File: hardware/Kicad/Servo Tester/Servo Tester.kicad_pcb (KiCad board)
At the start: 2 copper layers, 135 x 75 mm, 58 parts, among them J1 Servo 1, J2 Servo 2, J3 Servo 3, J4 XT60PW-M, SW1 SS-12D11, SW2 STD / HV, SW3 SW_Push - Up, SW4 SW_Push - Select, SW5 SW_Push - Down, U1 Mini360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

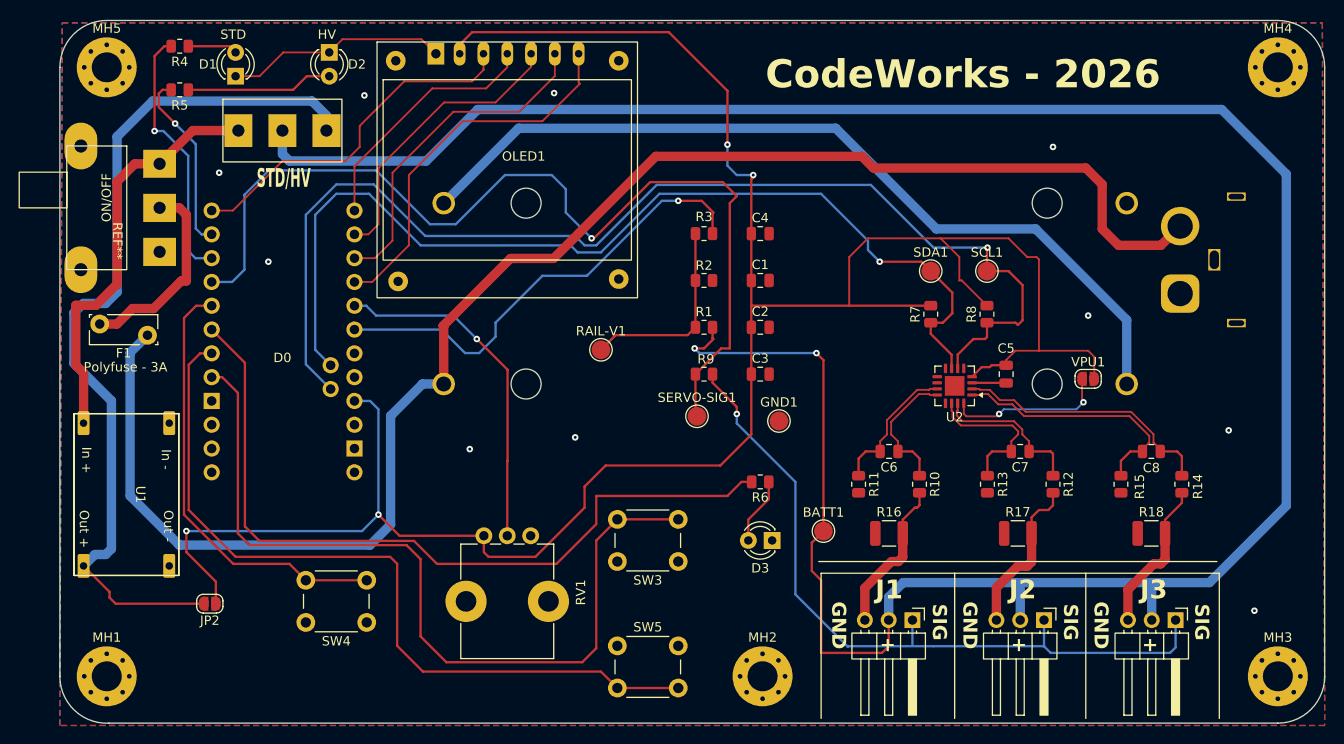
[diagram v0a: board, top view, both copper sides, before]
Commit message: Add designators, netlist, positions, and symbol library for Servo Tester project
- Created designators.csv to define component designators for the Servo Tester.
- Added netlist.ipc to specify the electrical connections and layout of the circuit.
- Introduced positions.csv to provide the coordinates and rotation for each component on the PCB.
- Established sym-lib-table to include the Servo Tester symbol library in KiCad.
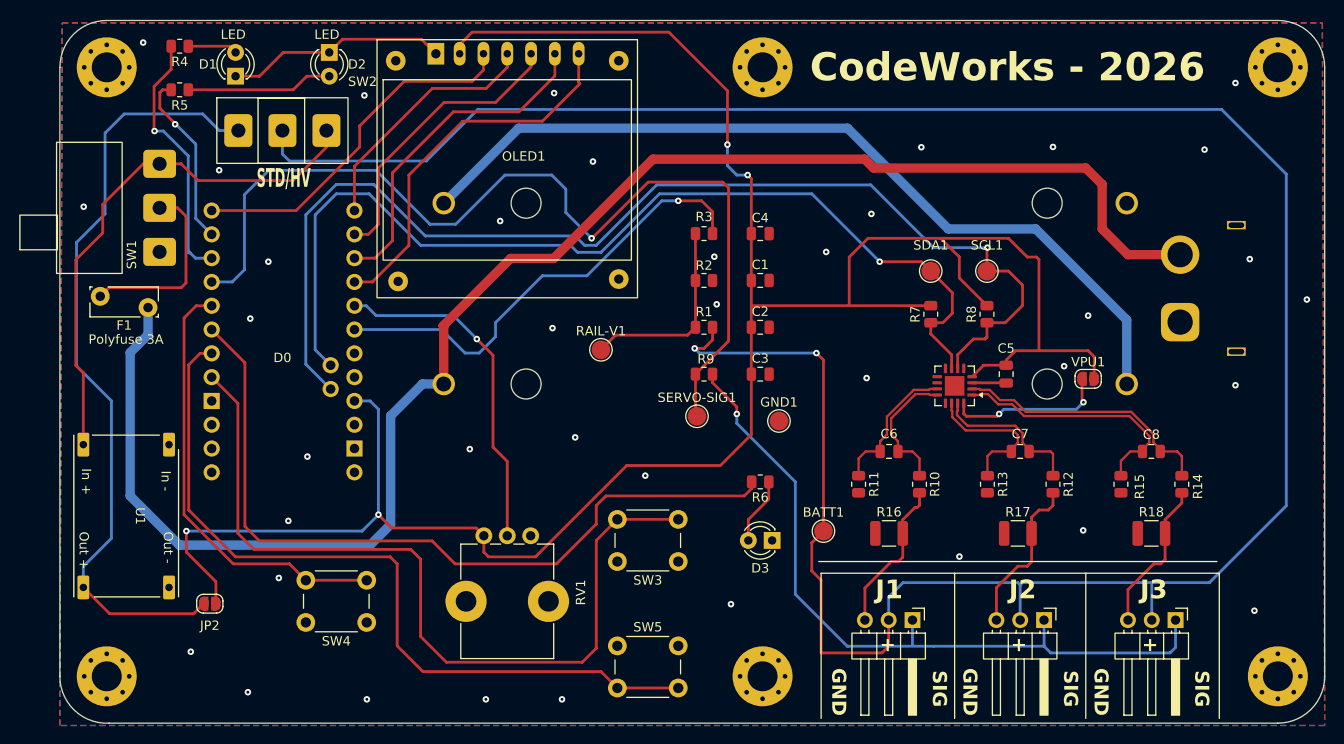
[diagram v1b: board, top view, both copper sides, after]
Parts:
- added MH6: ~, Servo Tester:MountingHole_3.2mm_M3_Pad_Via, F.Cu at (164.8, 60.8)
- A1: footprint CodeWorks-Essentials:Clone_Pro_Mini_Socket_No_PROG -> Servo Tester:Clone_Pro_Mini_Socket_No_PROG
- BATT1: value BATT -> TestPoint; footprint TestPoint:TestPoint_Pad_D2.0mm -> Servo Tester:TestPoint_Pad_D2.0mm
- BT1: footprint CodeWorks-Essentials:BAT_BK-18650-PC4 -> Servo Tester:BAT_BK-18650-PC4
- C1, C2, C5: value 100nF -> C; footprint Capacitor_SMD:C_0805_2012Metric -> Servo Tester:C_0805_2012Metric
- C3, C6, C8: value 0.1uF -> C; footprint Capacitor_SMD:C_0805_2012Metric -> Servo Tester:C_0805_2012Metric
- C4: value 10uF -> C; footprint Capacitor_SMD:C_0805_2012Metric -> Servo Tester:C_0805_2012Metric
- C7: value 0.1uf -> C; footprint Capacitor_SMD:C_0805_2012Metric -> Servo Tester:C_0805_2012Metric
- D1: value STD -> LED; footprint LED_THT:LED_D3.0mm -> Servo Tester:LED_D3.0mm
- D2: value HV -> LED; footprint LED_THT:LED_D3.0mm -> Servo Tester:LED_D3.0mm
- D3: value ALERT -> LED; footprint LED_THT:LED_D3.0mm -> Servo Tester:LED_D3.0mm
- F1: value Polyfuse - 3A -> Polyfuse 3A; footprint Fuse:Fuse_Bourns_MF-RG300 -> Servo Tester:Fuse_LittleFuseRUEF300
- GND1: value GND -> TestPoint; footprint TestPoint:TestPoint_Pad_D2.0mm -> Servo Tester:TestPoint_Pad_D2.0mm
- J1: value Servo 1 -> Conn_01x03_Pin; footprint Connector_PinHeader_2.54mm:PinHeader_1x03_P2.54mm_Horizontal -> Servo Tester:PinHeader_1x03_P2.54mm_Horizontal
- J2: value Servo 2 -> Conn_01x03_Pin; footprint Connector_PinHeader_2.54mm:PinHeader_1x03_P2.54mm_Horizontal -> Servo Tester:PinHeader_1x03_P2.54mm_Horizontal
- J3: value Servo 3 -> Conn_01x03_Pin; footprint Connector_PinHeader_2.54mm:PinHeader_1x03_P2.54mm_Horizontal -> Servo Tester:PinHeader_1x03_P2.54mm_Horizontal
- J4: footprint Connector_AMASS:AMASS_XT60IPW-M_1x03_P7.20mm_Horizontal -> Servo Tester:AMASS_XT60PW-M_1x02_P7.20mm_Horizontal
- JP2: value 5V -> SolderJumper_2_Open; footprint Jumper:SolderJumper-2_P1.3mm_Open_RoundedPad1.0x1.5mm -> Servo Tester:SolderJumper-2_P1.3mm_Open_RoundedPad1.0x1.5mm
- MH1, MH2, MH3, MH4, MH5: value M3 -> ~; footprint MountingHole:MountingHole_3.2mm_M3_Pad_Via -> Servo Tester:MountingHole_3.2mm_M3_Pad_Via
- OLED1: footprint CodeWorks-Essentials:OLED_0.96_SPI_Module_1x07_P2.54mm -> Servo Tester:OLED_0.96_SPI_Module_1x07_P2.54mm
- R1: value 47K -> R; footprint Resistor_SMD:R_0805_2012Metric -> Servo Tester:R_0805_2012Metric
- R10, R11, R12, R13, R14, R15: value 10R -> R; footprint Resistor_SMD:R_0805_2012Metric -> Servo Tester:R_0805_2012Metric
- R16, R17, R18: value 0.1R -> R; footprint Resistor_SMD:R_1210_3225Metric -> Servo Tester:R_1210_3225Metric
- R2: value 27K -> R; footprint Resistor_SMD:R_0805_2012Metric -> Servo Tester:R_0805_2012Metric
- R3: value 0R -> R; footprint Resistor_SMD:R_0805_2012Metric -> Servo Tester:R_0805_2012Metric
- R4, R5: value 1K -> R; footprint Resistor_SMD:R_0805_2012Metric -> Servo Tester:R_0805_2012Metric
- R6: value 470R -> R; footprint Resistor_SMD:R_0805_2012Metric -> Servo Tester:R_0805_2012Metric
- R7, R8: value 4.7K -> R; footprint Resistor_SMD:R_0805_2012Metric -> Servo Tester:R_0805_2012Metric
- R9: value 330R -> R; footprint Resistor_SMD:R_0805_2012Metric -> Servo Tester:R_0805_2012Metric
- RAIL-V1: value ~ -> TestPoint; footprint TestPoint:TestPoint_Pad_D2.0mm -> Servo Tester:TestPoint_Pad_D2.0mm
- RV1: footprint Potentiometer_THT:Potentiometer_Bourns_PTV09A-1_Single_Vertical -> Servo Tester:Potentiometer_Bourns_PTV09A-1_Single_Vertical
- SCL1: value SCL -> TestPoint; footprint TestPoint:TestPoint_Pad_D2.0mm -> Servo Tester:TestPoint_Pad_D2.0mm
- SDA1: value SDA -> TestPoint; footprint TestPoint:TestPoint_Pad_D2.0mm -> Servo Tester:TestPoint_Pad_D2.0mm
- SERVO-SIG1: value SERVO-SIG -> TestPoint; footprint TestPoint:TestPoint_Pad_D2.0mm -> Servo Tester:TestPoint_Pad_D2.0mm
- SW1: value SS-12D11 -> SS-12DXX; footprint CodeWorks-Essentials:SS-12D11 -> Servo Tester:SS12D11
- SW2: value STD / HV -> SS-12DXX; footprint CodeWorks-Essentials:SS-12D10 -> Servo Tester:SS12D10
- SW3: value SW_Push - Up -> SW_Push - Down; footprint Button_Switch_THT:SW_PUSH_6mm_H8.5mm -> Servo Tester:SW_PUSH_6mm_H8.5mm
- SW4: value SW_Push - Select -> SW_Push - Down; footprint Button_Switch_THT:SW_PUSH_6mm_H8.5mm -> Servo Tester:SW_PUSH_6mm_H8.5mm
- SW5: footprint Button_Switch_THT:SW_PUSH_6mm_H8.5mm -> Servo Tester:SW_PUSH_6mm_H8.5mm
- U1: footprint CodeWorks-Essentials:Ultra Mini-360 -> Servo Tester:Ultra Mini-360
- U2: footprint Package_DFN_QFN:Texas_RGV0016A_VQFN-16-1EP_4x4mm_P0.65mm_EP2.1x2.1mm -> Servo Tester:INA3221_VQFN-16_4x4mm_P0.65mm_EP2.6x2.6mm
- VPU1: value VPU -> SolderJumper_2_Open; footprint Jumper:SolderJumper-2_P1.3mm_Open_RoundedPad1.0x1.5mm -> Servo Tester:SolderJumper-2_P1.3mm_Open_RoundedPad1.0x1.5mm
- moved J4 3.05 mm to (209.3, 87.9)
- moved F1 2.96 mm to (99.2, 86.4)
- moved U1 2.29 mm to (96.8, 108.6)
- turned SW1 to 90 degrees
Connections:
- net Net-(BT1-Pad1-) renamed /BATT
- net Net-(J4-N) renamed /BATT+
- SW1 pad 1: Net-(F1-Pad2) -> unconnected-(SW1-Pad1)
- SW1 pad 2: Net-(U1-IN+) -> Net-(F1-Pad2)
- SW1 pad 3: unconnected-(SW1-Pad3) -> Net-(U1-IN+)
- SW2 pad 1: +BATT -> Net-(JP2-B)
- SW2 pad 2: Net-(U1-IN+) -> +BATT
- SW2 pad 3: Net-(JP2-B) -> Net-(U1-IN+)
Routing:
- net Net-(U1-IN+): track 44.4 -> 58.4 mm
- net Net-(JP2-B): track 93.7 -> 82.8 mm
- net /BATT+: track 167.4 -> 169.7 mm
- net +5V: track 248.2 -> 246.2 mm
- net Net-(F1-Pad2): track 21.4 -> 20.1 mm
- net /SERVO: track 103.5 -> 102.3 mm
- net /SCL: track 123.6 -> 122.5 mm
- net /HV: track 19.5 -> 18.8 mm
- net /BTN-UP: track 89.1 -> 88.4 mm
- net /SDA: track 106.5 -> 105.9 mm
- net GND: vias 10 -> 39

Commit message: feat: Add language selection and improve UI for servo tester
- Introduced compile-time language selection for English and Czech.
- Updated UI strings to use language-specific definitions.
- Added support for optional power mode indicator LEDs.
- Implemented burn cycles feature to limit servo sweep cycles.
- Enhanced settings storage and validation for new burn cycles parameter.
- Improved serial debug output for INA3221 communication checks.
- Updated display functions to reflect new settings and language changes.
- Adjusted pin configuration in documentation to match new features.
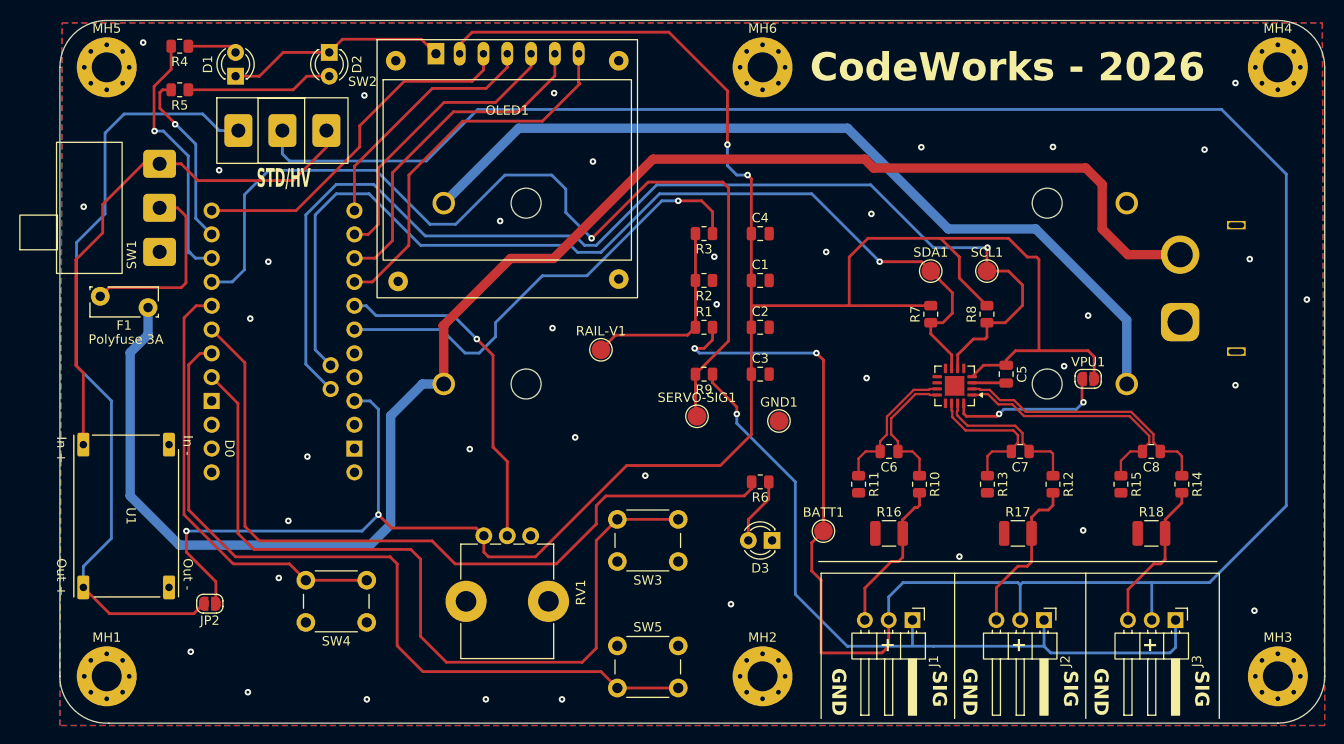
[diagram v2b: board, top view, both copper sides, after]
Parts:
- A1: footprint Servo Tester:Clone_Pro_Mini_Socket_No_PROG -> CodeWorks-Essentials:Clone_Pro_Mini_Socket_No_PROG
- BATT1, GND1, RAIL-V1, SCL1, SDA1, SERVO-SIG1: footprint Servo Tester:TestPoint_Pad_D2.0mm -> TestPoint:TestPoint_Pad_D2.0mm
- C1, C2, C5: value C -> 100nF; footprint Servo Tester:C_0805_2012Metric -> Capacitor_SMD:C_0805_2012Metric
- C3, C7, C8: value C -> 0.1uF; footprint Servo Tester:C_0805_2012Metric -> Capacitor_SMD:C_0805_2012Metric
- C4: value C -> 10uF; footprint Servo Tester:C_0805_2012Metric -> Capacitor_SMD:C_0805_2012Metric
- C6: value C -> 0.1nF; footprint Servo Tester:C_0805_2012Metric -> Capacitor_SMD:C_0805_2012Metric
- D1: value LED -> STD; footprint Servo Tester:LED_D3.0mm -> LED_THT:LED_D3.0mm
- D2: value LED -> HV; footprint Servo Tester:LED_D3.0mm -> LED_THT:LED_D3.0mm
- D3: value LED -> ALERT; footprint Servo Tester:LED_D3.0mm -> LED_THT:LED_D3.0mm
- F1: footprint Servo Tester:Fuse_LittleFuseRUEF300 -> CodeWorks-Essentials:Fuse_LittleFuseRUEF300
- J1: value Conn_01x03_Pin -> Servo 1; footprint Servo Tester:PinHeader_1x03_P2.54mm_Horizontal -> Connector_PinHeader_2.54mm:PinHeader_1x03_P2.54mm_Horizontal
- J2: value Conn_01x03_Pin -> Servo 2; footprint Servo Tester:PinHeader_1x03_P2.54mm_Horizontal -> Connector_PinHeader_2.54mm:PinHeader_1x03_P2.54mm_Horizontal
- J3: value Conn_01x03_Pin -> Servo 3; footprint Servo Tester:PinHeader_1x03_P2.54mm_Horizontal -> Connector_PinHeader_2.54mm:PinHeader_1x03_P2.54mm_Horizontal
- J4: footprint Servo Tester:AMASS_XT60PW-M_1x02_P7.20mm_Horizontal -> CodeWorks-Connectors:AMASS_XT60PW-M_1x02_P7.20mm_Horizontal
- JP2, VPU1: footprint Servo Tester:SolderJumper-2_P1.3mm_Open_RoundedPad1.0x1.5mm -> Jumper:SolderJumper-2_P1.3mm_Open_RoundedPad1.0x1.5mm
- MH1, MH2, MH3, MH4, MH5, MH6: footprint Servo Tester:MountingHole_3.2mm_M3_Pad_Via -> MountingHole:MountingHole_3.2mm_M3_Pad_Via
- OLED1: footprint Servo Tester:OLED_0.96_SPI_Module_1x07_P2.54mm -> CodeWorks-Essentials:OLED_0.96_SPI_Module_1x07_P2.54mm
- R1: value R -> 47K; footprint Servo Tester:R_0805_2012Metric -> Resistor_SMD:R_0805_2012Metric
- R10, R11, R12, R13, R14, R15: value R -> 10R; footprint Servo Tester:R_0805_2012Metric -> Resistor_SMD:R_0805_2012Metric
- R16, R17, R18: value R -> 0.1R; footprint Servo Tester:R_1210_3225Metric -> Resistor_SMD:R_1210_3225Metric
- R2: value R -> 27K; footprint Servo Tester:R_0805_2012Metric -> Resistor_SMD:R_0805_2012Metric
- R3: value R -> 0R; footprint Servo Tester:R_0805_2012Metric -> Resistor_SMD:R_0805_2012Metric
- R4, R5: value R -> 1K; footprint Servo Tester:R_0805_2012Metric -> Resistor_SMD:R_0805_2012Metric
- R6: value R -> 470R; footprint Servo Tester:R_0805_2012Metric -> Resistor_SMD:R_0805_2012Metric
- R7, R8: value R -> 4K7; footprint Servo Tester:R_0805_2012Metric -> Resistor_SMD:R_0805_2012Metric
- R9: value R -> 330R; footprint Servo Tester:R_0805_2012Metric -> Resistor_SMD:R_0805_2012Metric
- RV1: footprint Servo Tester:Potentiometer_Bourns_PTV09A-1_Single_Vertical -> CodeWorks-Potentiometers:Potentiometer_Bourns_PTV09A-1_Single_Vertical
- SW1: footprint Servo Tester:SS12D11 -> CodeWorks-Slide_Switches:SS12D11
- SW2: footprint Servo Tester:SS12D10 -> CodeWorks-Slide_Switches:SS12D10
- SW3: value SW_Push - Down -> SW_Push - Up
- SW4: value SW_Push - Down -> SW_Push - Select
- U1: footprint Servo Tester:Ultra Mini-360 -> CodeWorks-Essentials:Ultra Mini-360
